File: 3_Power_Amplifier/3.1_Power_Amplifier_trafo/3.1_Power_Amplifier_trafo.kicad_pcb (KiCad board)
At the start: 2 copper layers, 100 x 100 mm, 11 parts, among them P1 IN_SWITCHEO, P2 OUT_CON_CAP, P3 OUT_SIN_CAP, P4 IN_FUENTE_CONM, T1 TRANSFO-SO12

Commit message: AMPLIFICADOR DE POTENCIA_2 PCB_UNO
CON ISLETAS Y DISIPADORES VERTICALES
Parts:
- added P10: TIERRA_POT, Sockets_MOLEX_KK-System:Socket_MOLEX-KK-RM3-96mm_Lock_2pin_straight, F.Cu at (97.6, 42.1)
- added P5: ISLETA, libreria_Power_Amplifier_huellas:Pad_Via_5.1mm_TOR, F.Cu at (70.5, 129.0)
- added P6: ISLETA, libreria_Power_Amplifier_huellas:Pad_Via_5.1mm_TOR, F.Cu at (158.5, 129.0)
- added P7: ISLETA, libreria_Power_Amplifier_huellas:Pad_Via_5.1mm_TOR, F.Cu at (158.5, 41.0)
- added P8: ISLETA, libreria_Power_Amplifier_huellas:Pad_Via_5.1mm_TOR, F.Cu at (70.5, 41.0)
- added P9: IN_FUENTE_CONM, Sockets_MOLEX_KK-System:Socket_MOLEX-KK-RM3-96mm_Lock_2pin_straight, F.Cu at (89.4, 42.0)
- P1: footprint Sockets_MOLEX_KK-System:Socket_MOLEX-KK-RM3-96mm_Lock_4pin_straight -> Sockets_MOLEX_KK-System:Socket_MOLEX-KK-RM3-96mm_Lock_2pin_straight
- P4: value IN_FUENTE_CONM -> TIERRA_POT; footprint Sockets_MOLEX_KK-System:Socket_MOLEX-KK-RM3-96mm_Lock_4pin_straight -> Sockets_MOLEX_KK-System:Socket_MOLEX-KK-RM3-96mm_Lock_2pin_straight
- moved P4 86.8 mm to (96.9, 127.7), turned to 180 degrees
- moved P1 15.5 mm to (88.7, 127.8), turned to 180 degrees
- moved P2 8.39 mm to (157.2, 52.6)
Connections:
- P1 pad 1: /GND -> /SWITCHEO
- P1 pad 2: /GND -> /SWITCHEO
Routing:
- net /VDD: track 22.9 -> 0.00 mm
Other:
- board text added: "3_POWER AMPLIFIER PART 2"
- board text added: "GND"
- board text added: "SWITCHEO"
- board text added: "TRANSFORMADOR 1 : 13"
- board text added: "VDD"

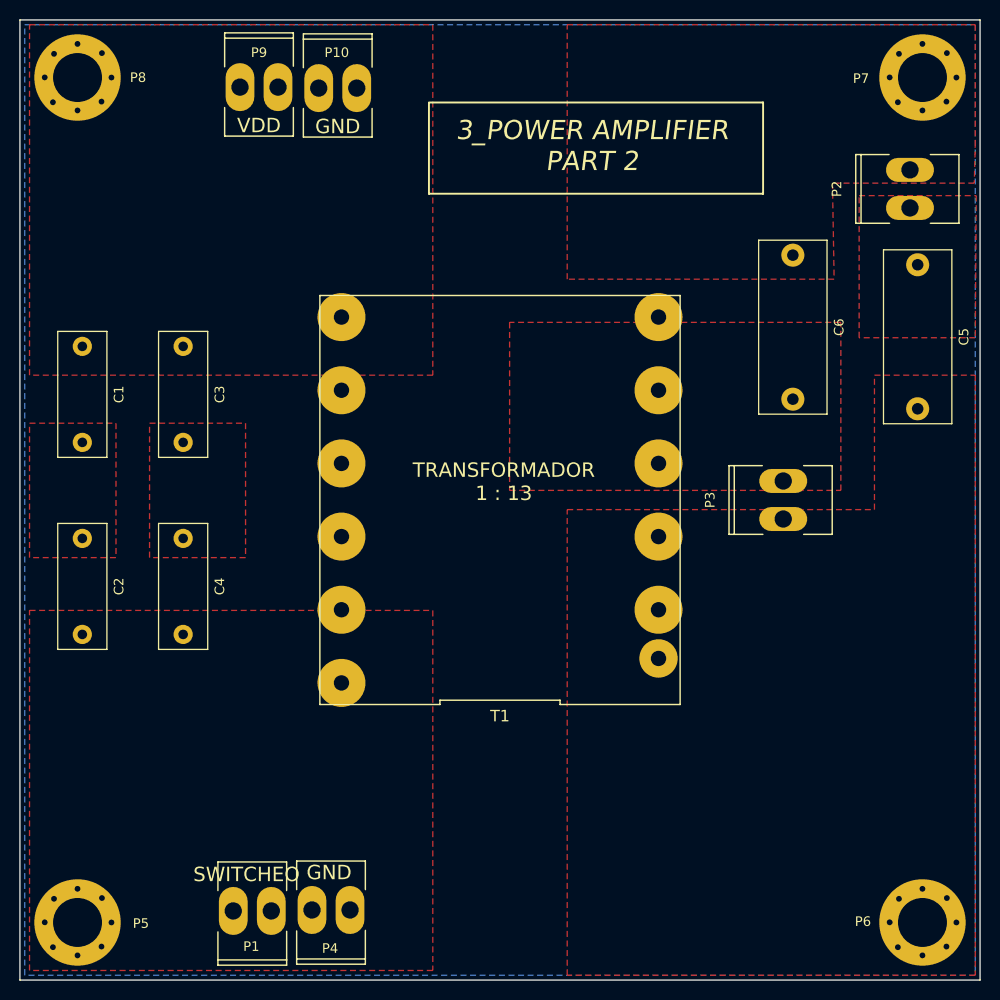
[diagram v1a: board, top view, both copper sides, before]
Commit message: AMPLIFICADOR DE POTENCIAS_2 PCB_V2
modificaciones a la pcb del trafo
falta arreglos a la pcb de los mosfet
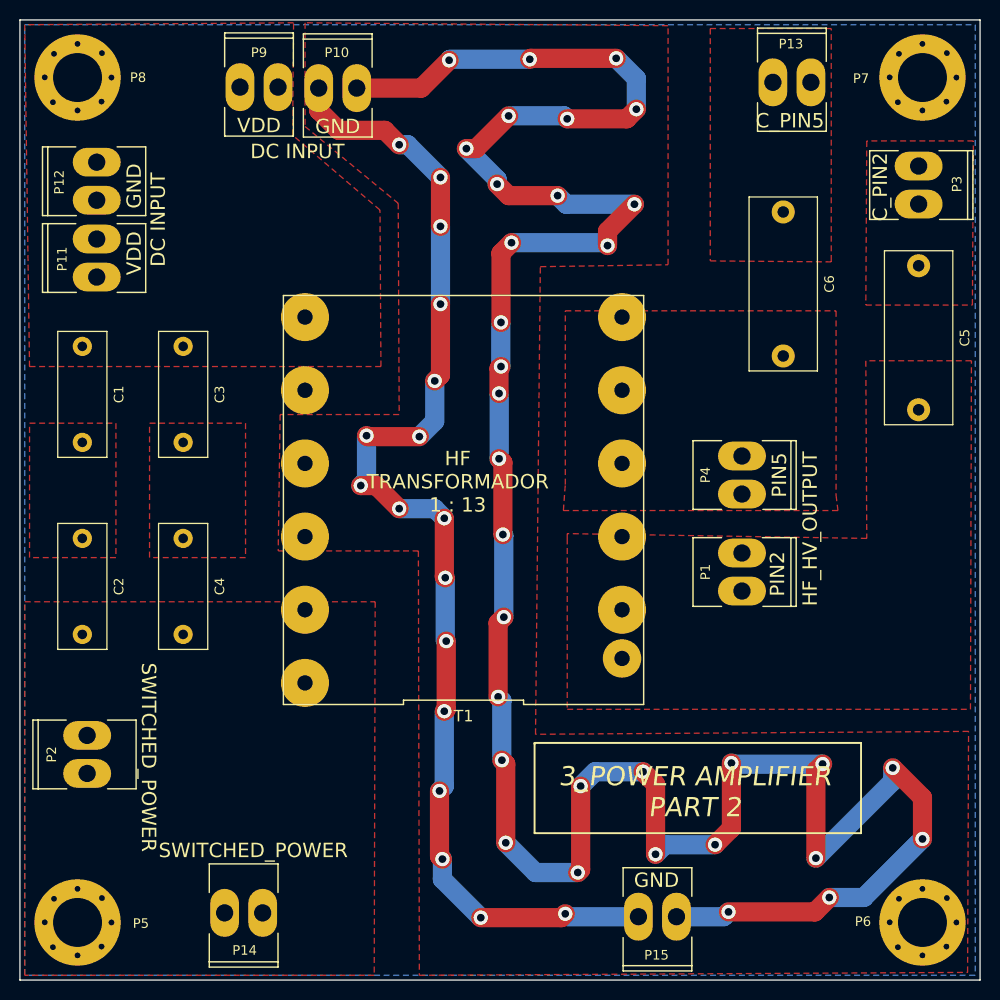
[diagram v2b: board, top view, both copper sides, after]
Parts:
- added P11: DC_INPUT, Sockets_MOLEX_KK-System:Socket_MOLEX-KK-RM3-96mm_Lock_2pin_straight, F.Cu at (72.5, 59.8)
- added P12: TIERRA_POT, Sockets_MOLEX_KK-System:Socket_MOLEX-KK-RM3-96mm_Lock_2pin_straight, F.Cu at (72.5, 51.8)
- added P13: CON_HF_HV_OUTPUT_P5, Sockets_MOLEX_KK-System:Socket_MOLEX-KK-RM3-96mm_Lock_2pin_straight, F.Cu at (144.9, 41.5)
- added P14: SWITCHED_POWER, Sockets_MOLEX_KK-System:Socket_MOLEX-KK-RM3-96mm_Lock_2pin_straight, F.Cu at (87.8, 128.0)
- added P15: TIERRA_POT, Sockets_MOLEX_KK-System:Socket_MOLEX-KK-RM3-96mm_Lock_2pin_straight, F.Cu at (130.9, 128.4)
- P1: value IN_SWITCHEO -> HF_HV_OUTPUT_P2
- P2: value OUT_CON_CAP -> SWITCHED_POWER; footprint libreria_Power_Amplifier_huellas:Socket_MOLEX-KK-RM3-96mm_Lock_2pin_straight -> Sockets_MOLEX_KK-System:Socket_MOLEX-KK-RM3-96mm_Lock_2pin_straight
- P3: value OUT_SIN_CAP -> CON_HF_HV_OUTPUT_P2; footprint libreria_Power_Amplifier_huellas:Socket_MOLEX-KK-RM3-96mm_Lock_2pin_straight -> Sockets_MOLEX_KK-System:Socket_MOLEX-KK-RM3-96mm_Lock_2pin_straight
- P4: value TIERRA_POT -> HF_HV_OUTPUT_P5
- P9: value IN_FUENTE_CONM -> DC_INPUT
- moved P2 104.0 mm to (71.5, 111.5)
- moved P4 62.3 mm to (139.7, 82.4), turned to 270 degrees
- moved P1 62.0 mm to (139.7, 92.5), turned to 270 degrees
- moved P3 35.7 mm to (158.1, 52.2), turned to 270 degrees
- moved C6 4.61 mm to (144.0, 55.0)
- moved T1 3.80 mm to (110.7, 85.0)
- moved C5 0.14 mm to (158.1, 60.6)
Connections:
- C2 pad 2: /SWITCHEO -> /SWITCHED_POWER
- C4 pad 2: /SWITCHEO -> /SWITCHED_POWER
- C5 pad 1: /H_V_TWO -> /CON_HF_HV_P2
- C5 pad 2: /OUT_POT_TWO -> /HF_HV_OUTPUT_P2
- C6 pad 1: /H_V_ONE -> /CON_HF_HV_P5
- C6 pad 2: /OUT_POT_ONE -> /HF_HV_OUTPUT_P5
- P1 pad 1: /SWITCHEO -> /HF_HV_OUTPUT_P2
- P1 pad 2: /SWITCHEO -> /HF_HV_OUTPUT_P2
- P2 pad 1: /H_V_TWO -> /SWITCHED_POWER
- P2 pad 2: /H_V_ONE -> /SWITCHED_POWER
- P3 pad 1: /OUT_POT_TWO -> /CON_HF_HV_P2
- P3 pad 2: /OUT_POT_ONE -> /CON_HF_HV_P2
- P4 pad 1: /GND -> /HF_HV_OUTPUT_P5
- P4 pad 2: /GND -> /HF_HV_OUTPUT_P5
- T1 pad 12: /SWITCHEO -> /SWITCHED_POWER
- T1 pad 2: /OUT_POT_TWO -> /HF_HV_OUTPUT_P2
- T1 pad 5: /OUT_POT_ONE -> /HF_HV_OUTPUT_P5
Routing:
- net /GND: track 0.00 -> 401.1 mm, vias 0 -> 50
- added copper zone on F.Cu, net /CON_HF_HV_P2
- added copper zone on F.Cu, net /CON_HF_HV_P5
- added copper zone on F.Cu, net /GND
- added copper zone on F.Cu, net /HF_HV_OUTPUT_P2
- added copper zone on F.Cu, net /HF_HV_OUTPUT_P5
- added copper zone on F.Cu, net /SWITCHED_POWER
- removed copper zone on F.Cu, net /H_V_ONE
- removed copper zone on F.Cu, net /H_V_TWO
- removed copper zone on F.Cu, net /OUT_POT_ONE
- removed copper zone on F.Cu, net /OUT_POT_TWO
- removed copper zone on F.Cu, net /SWITCHEO
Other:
- board text added: "C_PIN2"
- board text added: "C_PIN5"
- board text added: "DC INPUT"
- board text added: "HF TRANSFORMADOR 1 : 13"
- board text added: "HF_HV_OUTPUT"
- board text added: "PIN2"
- board text added: "PIN5"
- board text added: "SWITCHED_POWER"
- board text removed: "SWITCHEO"
- board text removed: "TRANSFORMADOR 1 : 13"

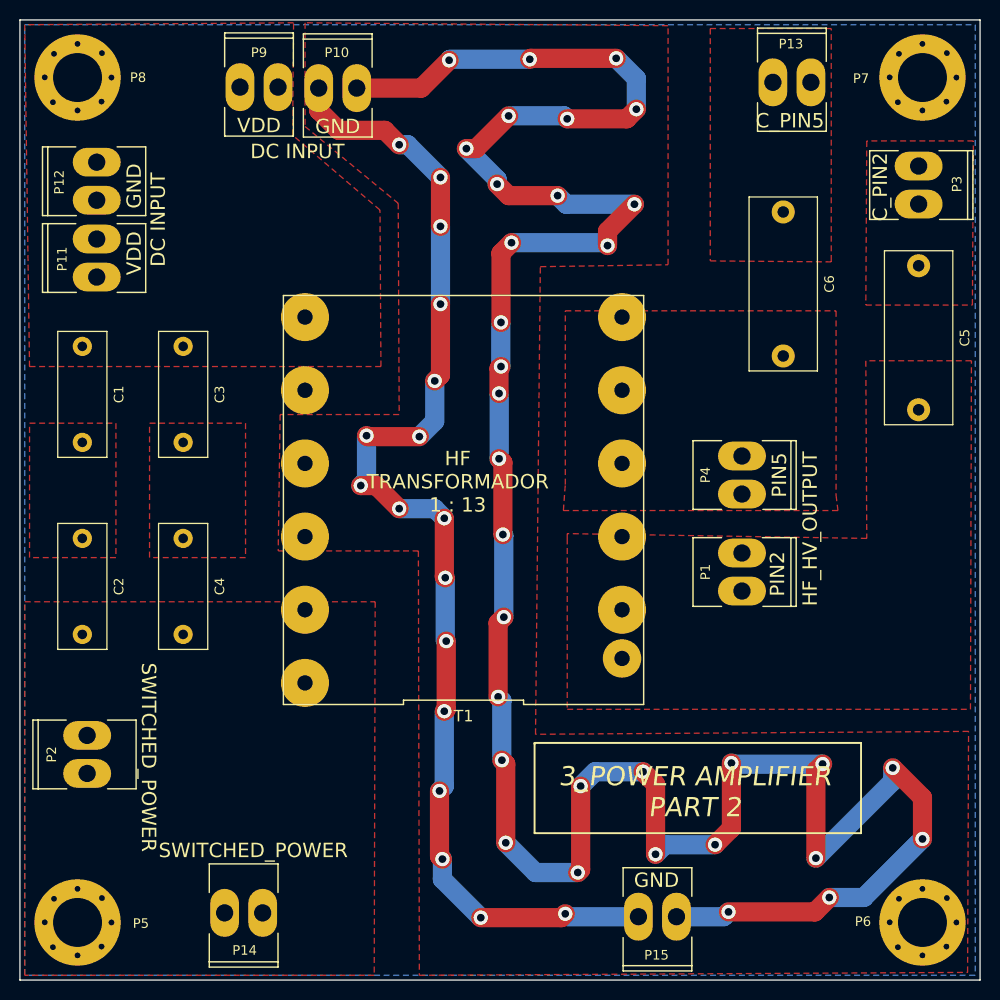
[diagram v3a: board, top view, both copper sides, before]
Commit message: AMPLIFICADOR DE POTENCIA_2 PCB_V5
LLENADO DE VIAS Y PLANOS PARA SOLDAR
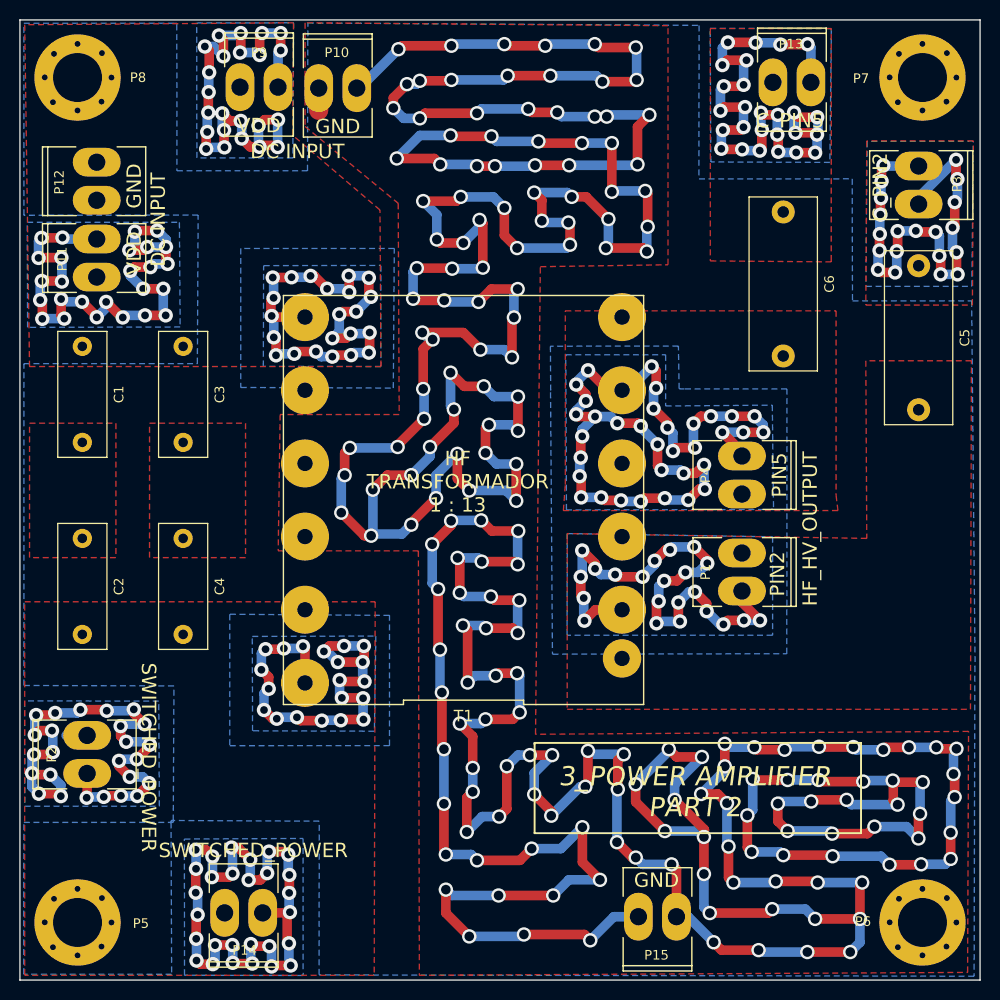
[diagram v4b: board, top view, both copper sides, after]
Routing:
- net /GND: track 401.1 -> 829.6 mm, vias 50 -> 194
- net /SWITCHED_POWER: track 0.00 -> 173.6 mm, vias 0 -> 73
- net /VDD: track 0.00 -> 164.7 mm, vias 0 -> 71
- net /HF_HV_OUTPUT_P5: track 0.00 -> 88.7 mm, vias 0 -> 34
- net /CON_HF_HV_P5: track 0.00 -> 63.4 mm, vias 0 -> 26
- net /HF_HV_OUTPUT_P2: track 0.00 -> 58.7 mm, vias 0 -> 22
- net /CON_HF_HV_P2: track 0.00 -> 50.2 mm, vias 0 -> 20
- added copper zone on B.Cu, net /CON_HF_HV_P2
- added copper zone on B.Cu, net /CON_HF_HV_P5
- added copper zone on B.Cu, net /HF_HV_OUTPUT_P2
- added copper zone on B.Cu, net /HF_HV_OUTPUT_P5
- added copper zone on B.Cu, net /SWITCHED_POWER
- added copper zone on B.Cu, net /VDD

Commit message: GENERADOR_V8
ORGANIZACION DE ELEMENTOS
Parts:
- P5, P6, P7, P8: footprint libreria_Power_Amplifier_huellas:Pad_Via_5.1mm_TOR -> Mounting_Holes:MountingHole_3.2mm_M3_Pad_Via
- moved P5 1.41 mm to (69.5, 130.0)
- moved P6 1.41 mm to (159.5, 130.0)
- moved P7 1.41 mm to (159.5, 40.0)
- moved P8 1.41 mm to (69.5, 40.0)
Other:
- net class vias_potencia added: clearance 0.3, trace_width 0.25, via_dia 0.6, via_drill 0.4

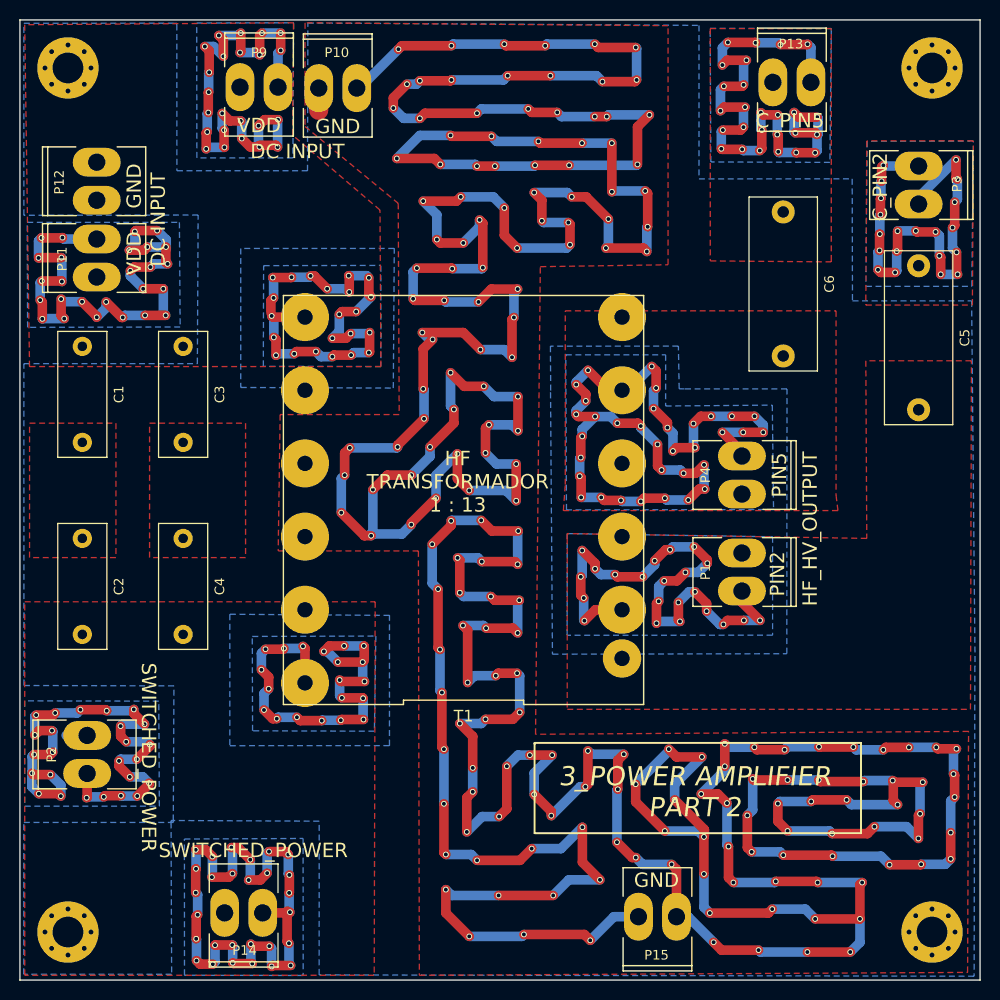
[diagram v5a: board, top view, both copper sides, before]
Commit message: GENERADOR V11
TRAZADO DE PISTAS Y VIAS
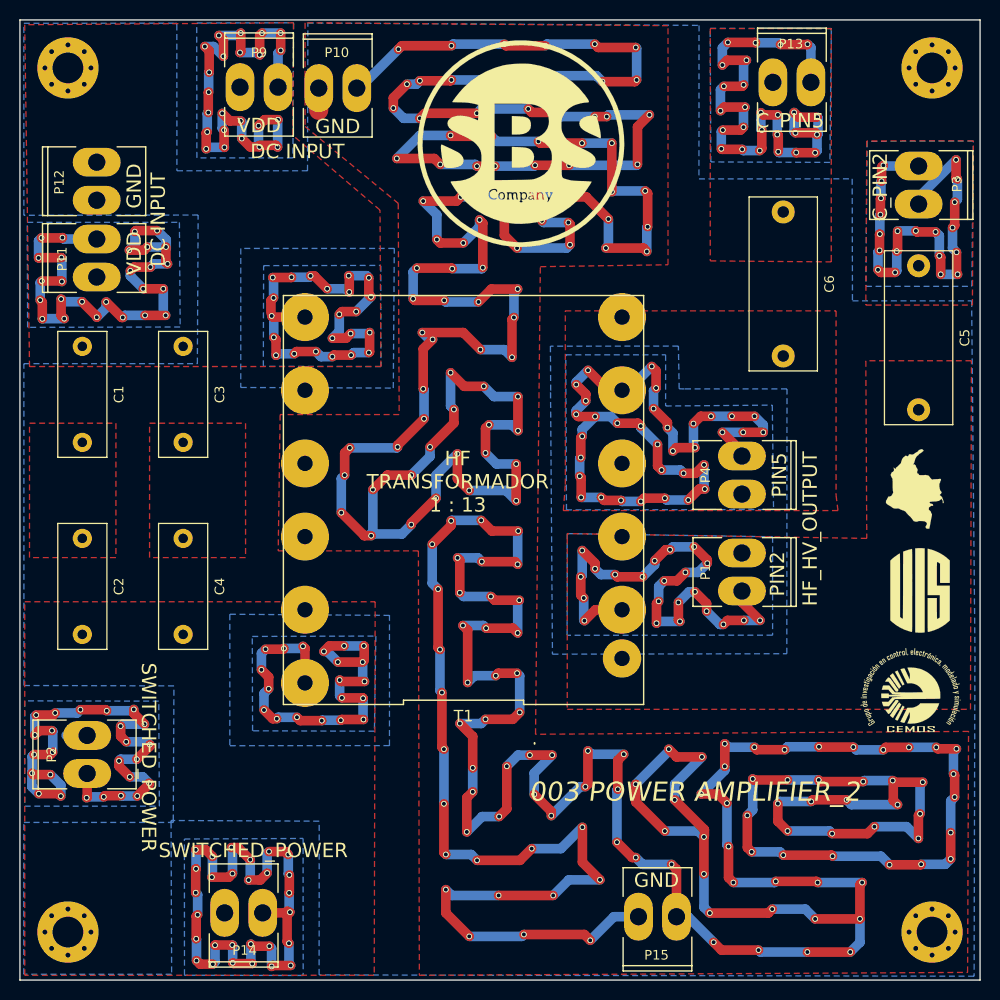
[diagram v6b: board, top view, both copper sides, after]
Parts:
- added G***: LOGO, Logos_Fuentes:Colombia, F.Cu at (157.8, 84.0)
- added G***: LOGO, Logos_Fuentes:SBS_22mm, F.Cu at (116.7, 47.9)
- added G***: LOGO, Logos_Fuentes:UIS, F.Cu at (158.2, 94.4)
- added G***: LOGO, Logos_Fuentes:CMOS, F.Cu at (157.2, 104.8)
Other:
- board text added: "003 POWER AMPLIFIER_2"
- board text removed: "3_POWER AMPLIFIER PART 2"
